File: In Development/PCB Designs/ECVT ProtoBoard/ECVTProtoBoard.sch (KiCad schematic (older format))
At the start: 28 parts, among them J1 Motor Driver, J10 Conn_01x08, J11 5V, J12 Hall Effect, J13 Hall Effect, J14 External Power Switch, J15 Conn_01x08, J16 MotorDriver2, J18 3V3, J19 GND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

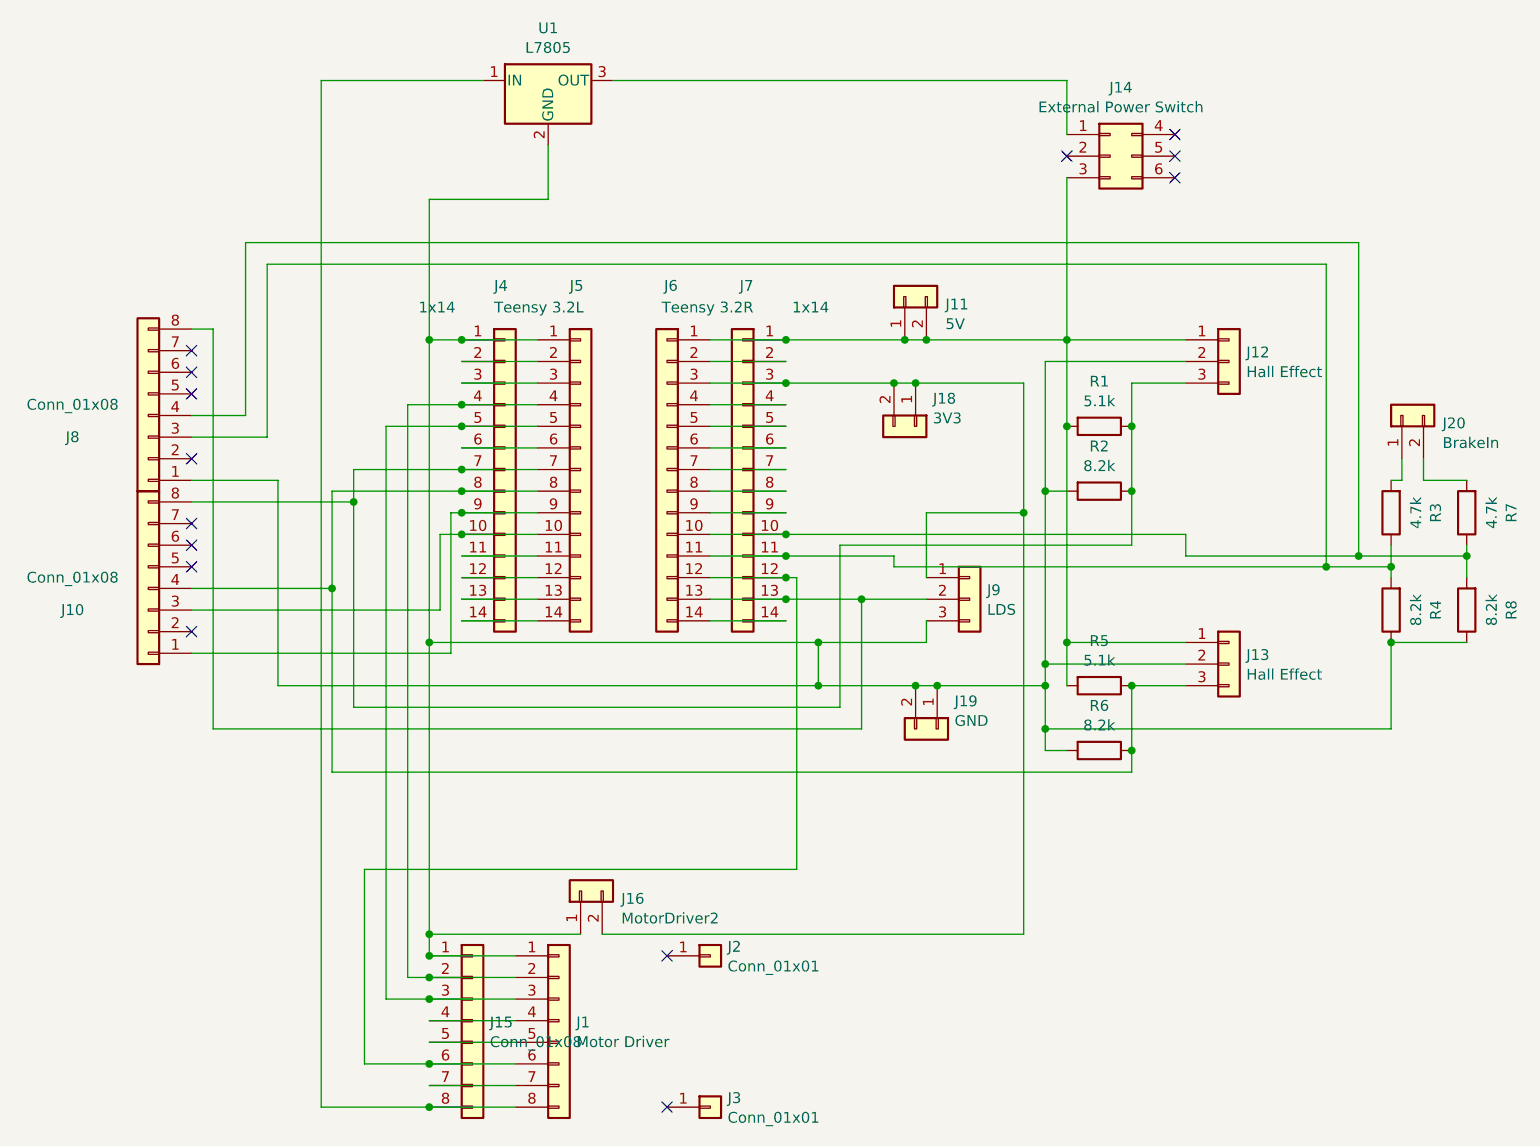
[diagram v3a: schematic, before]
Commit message: Finished DAQ and eCVT PCBs rev 2.1. Ready for ordering from JLCPCB
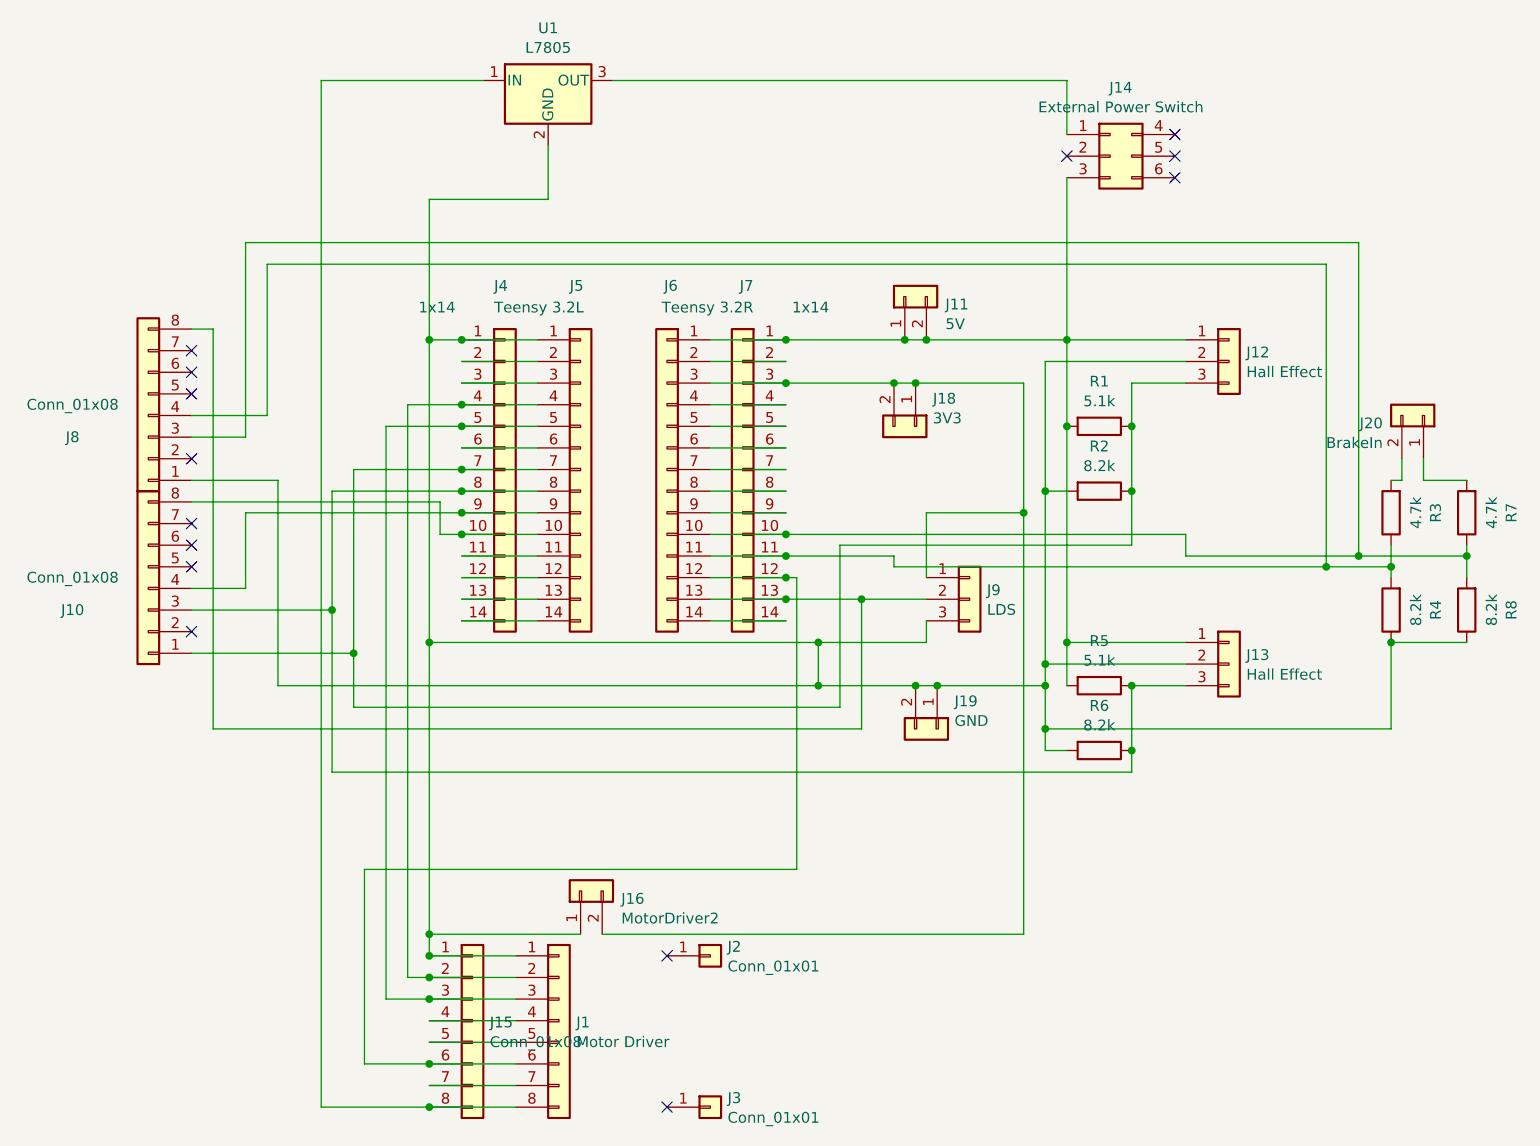
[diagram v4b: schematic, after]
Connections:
- net at J13.3 (Pin_3), J4.8 (Pin_8), J5.8 (Pin_8)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: now also J10.3 (Pin_3); no longer J10.4 (Pin_4)
- net at J12.3 (Pin_3), J4.7 (Pin_7), J5.7 (Pin_7)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: now also J10.1 (Pin_1); no longer J10.8 (Pin_8)
- net at J6.11 (Pin_11), J7.11 (Pin_11), R3.1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: now also J8.4 (Pin_4); no longer J8.3 (Pin_3)
- net at J6.10 (Pin_10), J7.10 (Pin_10), R7.1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: now also J8.3 (Pin_3); no longer J8.4 (Pin_4)
- net at J4.9 (Pin_9), J5.9 (Pin_9): now also J10.4 (Pin_4); no longer J10.1 (Pin_1)
- net at J4.10 (Pin_10), J5.10 (Pin_10): now also J10.8 (Pin_8); no longer J10.3 (Pin_3)
- net at R3.2: now also J20.2 (Pin_2); no longer J20.1 (Pin_1)
- net at R7.2: now also J20.1 (Pin_1); no longer J20.2 (Pin_2)
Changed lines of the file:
@@
 	6200 4650 3950 4650
-Wire Wire Line
-	3950 4650 3950 3700
 Wire Wire Line
 	3950 3550 4450 3550
 Connection ~ 7550 3650
 Connection ~ 4450 3550
-Wire Wire Line
-	3850 4950 3850 4100
 Wire Wire Line
 	3850 3650 4450 3650
@@
 Connection ~ 6100 4550
 Wire Wire Line
-	3850 4100 3200 4100
-Connection ~ 3850 4100
-Wire Wire Line
-	3850 4100 3850 3650
-Wire Wire Line
-	3950 3700 3200 3700
-Connection ~ 3950 3700
-Wire Wire Line
-	3950 3700 3950 3550
-Wire Wire Line
 	6300 4150 6300 4750
 Connection ~ 6300 4150
@@
 L Connector_Generic:Conn_01x02 J20
 U 1 1 5E2EAEE4
-P 8800 3300
-F 0 "J20" V 8764 3112 50  0000 R CNN
-F 1 "BrakeIn" V 8673 3112 50  0000 R CNN
-F 2 "CustomKiCADLibrary:PinHeader_1x02_P5.08mm_Vertical" H 8800 3300 50  0001 C CNN
-F 3 "~" H 8800 3300 50  0001 C CNN
-	1    8800 3300
-	0    -1   -1   0
+P 8900 3300
+F 0 "J20" V 8864 3112 50  0000 R CNN
+F 1 "BrakeIn" V 8773 3112 50  0000 R CNN
+F 2 "CustomKiCADLibrary:PinHeader_1x02_P5.08mm_Vertical" H 8900 3300 50  0001 C CNN
+F 3 "~" H 8900 3300 50  0001 C CNN
+	1    8900 3300
+	0    1    -1   0
 $EndComp
 $Comp
@@
 Wire Wire Line
 	8450 2600 3550 2600
-Wire Wire Line
-	3550 2600 3550 3400
-Wire Wire Line
-	3550 3400 3200 3400
 Connection ~ 8450 4000
 Wire Wire Line
@@
 Wire Wire Line
 	8600 2500 3450 2500
-Wire Wire Line
-	3450 2500 3450 3300
-Wire Wire Line
-	3450 3300 3200 3300
 Connection ~ 8600 3950
 Wire Wire Line
@@
 	5950 2950 6500 2950
 Wire Wire Line
-	3200 4200 4350 4200
-Wire Wire Line
-	3200 4400 4400 4400
-Wire Wire Line
-	4350 4200 4350 3850
-Wire Wire Line
 	4350 3850 4450 3850
 Connection ~ 4450 3850
-Wire Wire Line
-	4400 4400 4400 3750
-Wire Wire Line
-	4400 3750 4450 3750
 Connection ~ 4450 3750
+Wire Wire Line
+	3850 3650 3850 4200
+Wire Wire Line
+	3450 3750 3450 4100
+Wire Wire Line
+	3450 4100 3200 4100
+Wire Wire Line
+	3450 3750 4450 3750
+Wire Wire Line
+	4350 3850 4350 3700
+Wire Wire Line
+	4350 3700 3200 3700
+Wire Wire Line
+	3950 3550 3950 4400
+Wire Wire Line
+	3850 4200 3200 4200
+Connection ~ 3850 4200
+Wire Wire Line
+	3850 4200 3850 4950
+Wire Wire Line
+	3200 4400 3950 4400
+Connection ~ 3950 4400
+Wire Wire Line
+	3950 4400 3950 4650
+Wire Wire Line
+	3450 3400 3200 3400
+Wire Wire Line
+	3450 2500 3450 3400
+Wire Wire Line
+	3550 3300 3200 3300
+Wire Wire Line
+	3550 2600 3550 3300
 $EndSCHEMATC
